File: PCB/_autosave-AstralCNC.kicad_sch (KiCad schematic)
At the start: 47 parts, among them J1 USB_C_Receptacle_USB2.0_16P, J11 Conn_01x02, J31 Conn_01x10_Pin, J310 Conn_02x04_Counter_Clockwise, J311 Conn_01x04_Pin, J312 Conn_01x04_Pin, J313 Conn_01x04_Pin, J32 Conn_01x04_Pin, J33 Conn_01x03_Pin, J34 Conn_01x03_Pin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

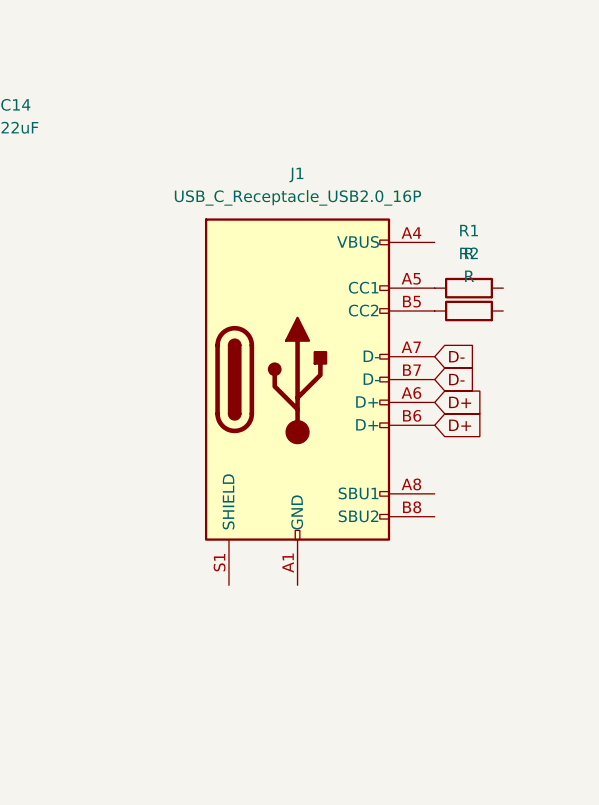
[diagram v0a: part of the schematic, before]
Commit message: Update journal entries: Adjusted hours for June 17 and June 19, added USB-C connector details, and included an image for clarity.
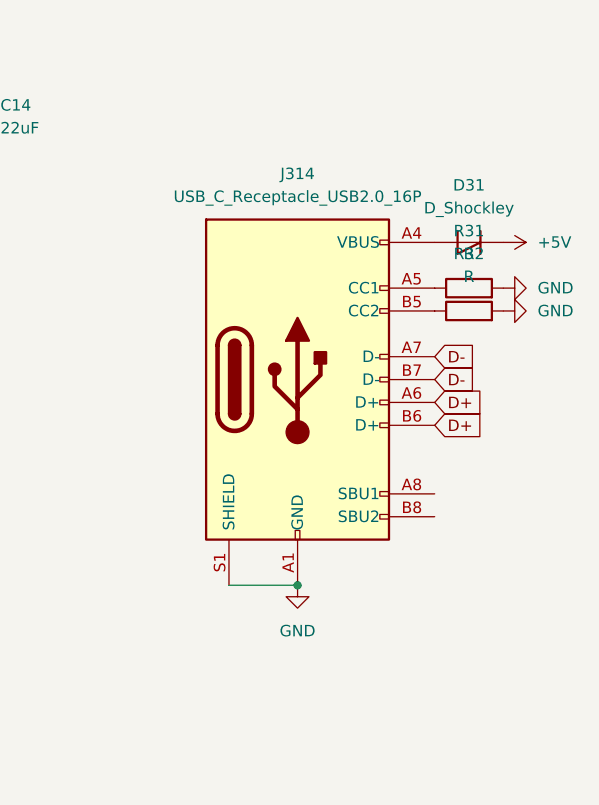
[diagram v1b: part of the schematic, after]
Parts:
- added D31: D_Shockley, symbol Device:D_Shockley
- renumbered J1 to J314, R1 to R31, R2 to R32
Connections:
- net +5V: now also D31.1 (K)
- net GND: now also J314.A1 (GND), J314.A12 (GND), J314.B1 (GND), J314.B12 (GND), J314.S1 (SHIELD), R31.2, R32.2
- net at J314.A4 (VBUS), J314.A9 (VBUS), J314.B4 (VBUS)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: now also D31.2 (A)
